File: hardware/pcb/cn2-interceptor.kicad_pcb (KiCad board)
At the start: 2 copper layers, 31.5 x 26 mm, 6 parts, among them J1 JST-XH 4P (CONTROLLER), J2 JST-XH 4P (PANEL), J3 JST-XH 3P (FLOW METER), J4 JST-XH 3P (FV TO CONTROLLER), U1 XIAO ESP32-C3, U2 4CH BSS138 LEVEL SHIFTER

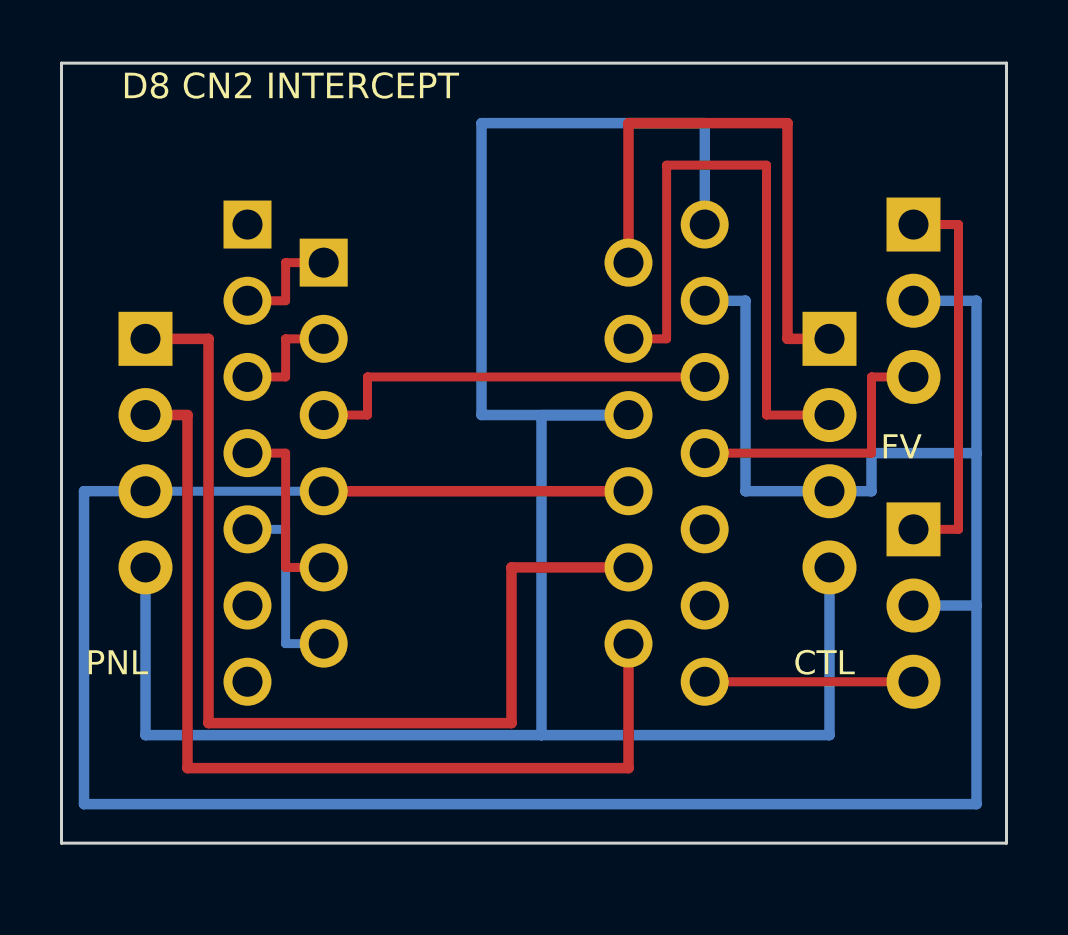
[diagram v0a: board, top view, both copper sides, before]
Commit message: pcb: 18.6 x 27 mm — connectors on opposite edges, flow relay dropped
39% less area and 41% narrower than the 31.5 x 26 board, which is the
dimension that decides whether it fits inside the appliance. Nothing about
the CN2 interception changes.

What made it small: the XIAO's two pad rows are 15.24 mm apart, so anything
standing beside them adds width directly, and the old board had a connector
on each side. Moving both to the top and bottom edges leaves nothing outside
the module except one routing lane -- shared by +5V on top and GND on the
bottom -- so the width is now pad block + lane + two edges, fully accounted
for and with nothing left in it. Each CN2 signal pin sits directly under the
middle corridor and climbs straight out of its own pad into its shifter pin,
turning once, so the four signals need no side lane at all.

The flow-meter relay (J3/J4) is gone, per Kai's call. Its six pins could not
share an edge with the CN2 connectors, so they were what forced the
connectors back onto the sides: that one feature cost more board than
everything else on it. The two hard-won warnings about it (the C3 is not 5 V
tolerant with no channel left to shift FV, and cutting the line strands the
meter's pull-up on the far side) are kept in the README for whoever re-adds
it.

Which connector goes on which edge is load-bearing, not cosmetic. Routing
forces LV1..LV4 onto D1..D4 in order -- they share a 0.94 mm channel and any
other order overlaps four deep -- and D1..D4 are GPIO3,4,5,6. The firmware's
as-built map puts the controller on GPIO5/6, which are the shifter's upper
channels, so the controller enters from the top. Get it backwards and the
board still works but only after swapping four defines, and a pin map that
disagrees with the copper does not announce itself: frames just stop
decoding. gen_pcb.py now reads firmware/include/config.h and fails on a
mismatch rather than leaving that to a comment.

Two new checks, both of which caught something real:

  MECHANICAL  th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
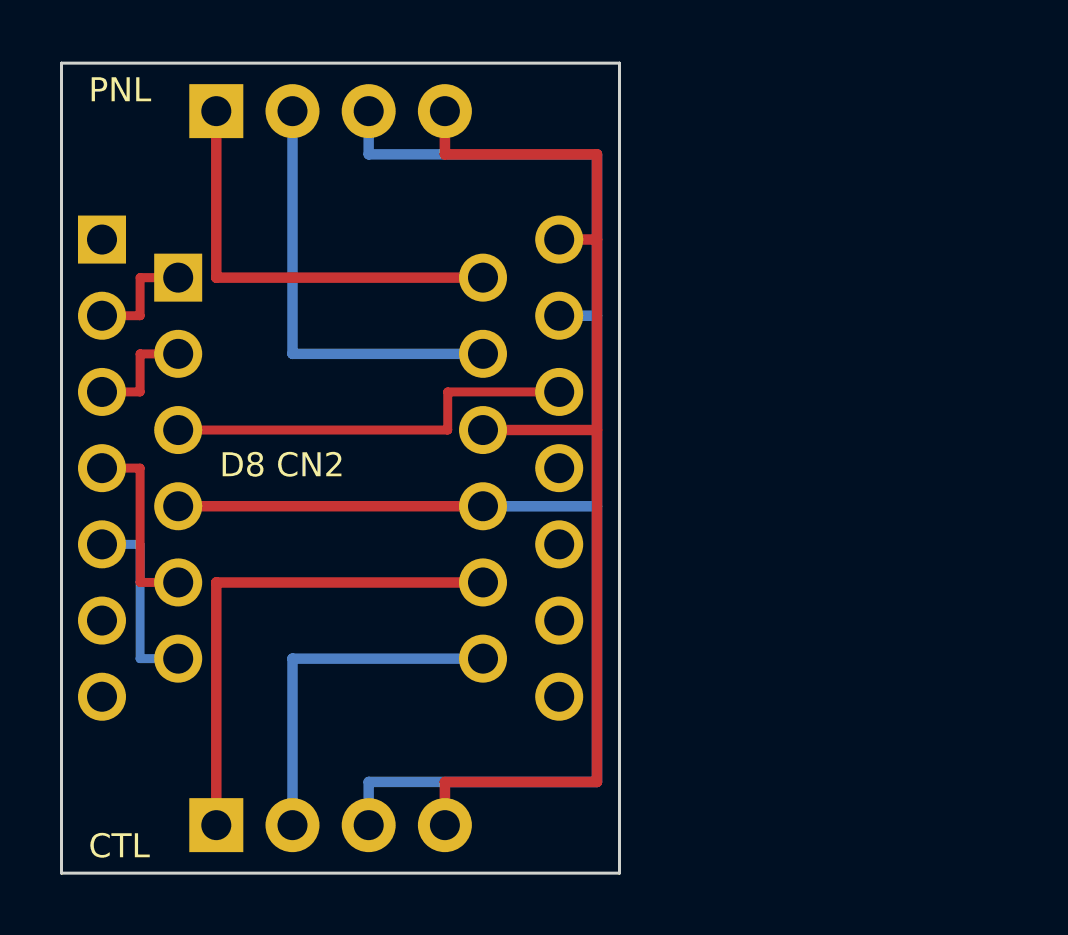
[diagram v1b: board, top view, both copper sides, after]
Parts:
- removed J3: JST-XH 3P (FLOW METER), cn2interceptor:JST_XH_3
- removed J4: JST-XH 3P (FV TO CONTROLLER), cn2interceptor:JST_XH_3
- moved J1 26.1 mm to (5.16, 25.4)
- moved J2 7.95 mm to (5.16, 1.60)
- moved U1 4.88 mm to (1.35, 5.88)
- moved U2 4.88 mm to (3.89, 7.15)
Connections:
- J1 pad 1: CH1_HV -> CH3_HV
- J1 pad 2: CH2_HV -> CH4_HV
- J2 pad 1: CH3_HV -> CH1_HV
- J2 pad 2: CH4_HV -> CH2_HV
- U1 pad D10: FLOW_IN -> (no net)
- U1 pad D7: FLOW_OUT -> (no net)
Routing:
- net GND: track 96.0 -> 54.2 mm
- net +5V: track 73.0 -> 39.0 mm
- net CH4_HV: track 32.0 -> 11.9 mm
- net CH3_HV: track 34.1 -> 17.0 mm
- net FV_VCC: track 13.2 -> 0.00 mm
- net FLOW_IN: track 9.50 -> 0.00 mm
- net FLOW_OUT: track 6.96 -> 0.00 mm
- net CH2_HV: track 20.8 -> 14.4 mm
- net CH1_HV: track 18.5 -> 14.4 mm
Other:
- board size 31.5 x 26 mm -> 18.6 x 27 mm
- board text added: "D8 CN2"
- board text removed: "D8 CN2 INTERCEPT"
- board text removed: "FV"

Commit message: pcb: silkscreen marks the XIAO's USB end and the JST latch side
Two orientation mistakes this board could not previously warn you about, both
of which look correct after assembly:

  USB + arrow   D0 and 5V are the pins at the XIAO's USB end and both sit at
                the low-y end here, so the port faces the PANEL connector.
                A 2x7 header is physically symmetric, so nothing stops the
                module going in backwards -- every signal then lands on the
                wrong pin.
  [ ] bracket   An XH shroud is not symmetric; the ramp the cable clip engages
                is on one long side. Both connectors are marked with the latch
                facing the nearest board edge, so the clips stay reachable once
                the board is mounted. Backwards, the clip faces the board and
                cannot be released.

The silkscreen engine could only draw glyphs, so this adds a Line primitive
and teaches both exporters about it -- the marks would otherwise have appeared
in my Gerbers and the panel but not in the .brd/.kicad_pcb that actually get
imported.

New silk_check(): silkscreen must stay on the board and off every pad. It
caught its own first draft -- the bracket ticks turned outward and ran 0.23 mm
past the edge, where the fab would simply have dropped them. Also bumped the
USB text to 0.8 mm, KiCad's minimum silk height.

Documented while marking it: the USB port faces J2 about 1.4 mm away. On
sockets it clears the JST housing, but a MATED panel cable stands about as
tall as the USB plug and sits right in front. Plug USB in first, or move both
connectors to the top edge (~21 x 24 mm, same area, USB clear). Worth naming
because a session on this project ran entirely over USB serial with the radio
off, so losing USB access after assembly is a real cost.

DRC PASS, connectivity PASS, mechanical PASS, KiCad DRC back to the 4 known
lib_footprint_issues, panel regenerated.

Co-Authored-By: Claude Opus 5 <noreply@anthropic.com>
Cl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
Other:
- board text added: "USB"
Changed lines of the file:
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@@
+      (net 1 "+5V"))
+  )
+  (footprint "cn2interceptor:JST_XH_4" (layer "F.Cu")
+    (at 5.16 25.4)
+    (fp_text reference "J1" (at 0 0) (layer "F.Fab")
+        (effects (font (size 1.27 1.27) (thickness 0.15)))
+    )
+    (fp_text value "JST-XH 4P (CONTROLLER)" (at 0 0) (layer "F.Fab")
+        (effects (font (size 1.27 1.27) (thickness 0.15)))
+    )
+    (pad "1" thru_hole rect (at 0 0) (size 1.8 1.8) (drill 1) (layers "*.Cu" "*.Mask")
+      (net 8 "CH3_HV") (thermal_bridge_angle 45))
+    (pad "2" thru_hole circle (at 2.54 0) (size 1.8 1.8) (drill 1) (layers "*.Cu" "*.Mask")
+      (net 10 "CH4_HV"))
+    (pad "3" thru_hole circle (at 5.08 0) (size 1.8 1.8) (drill 1) (layers "*.Cu" "*.Mask")
+      (net 2 "GND"))
+    (pad "4" thru_hole circle (at 7.62 0) (size 1.8 1.8) (drill 1) (layers "*.Cu" "*.Mask")
       (net 1 "+5V"))
   )
@@
       (net 11 "CH4_LV"))
   )
-  (footprint "cn2interceptor:JST_XH_4" (layer "F.Cu")
-    (at 5.16 25.4)
-    (fp_text reference "J1" (at 0 0) (layer "F.Fab")
-        (effects (font (size 1.27 1.27) (thickness 0.15)))
-    )
-    (fp_text value "JST-XH 4P (CONTROLLER)" (at 0 0) (layer "F.Fab")
-        (effects (font (size 1.27 1.27) (thickness 0.15)))
-    )
-    (pad "1" thru_hole rect (at 0 0) (size 1.8 1.8) (drill 1) (layers "*.Cu" "*.Mask")
-      (net 8 "CH3_HV") (thermal_bridge_angle 45))
-    (pad "2" thru_hole circle (at 2.54 0) (size 1.8 1.8) (drill 1) (layers "*.Cu" "*.Mask")
-      (net 10 "CH4_HV"))
-    (pad "3" thru_hole circle (at 5.08 0) (size 1.8 1.8) (drill 1) (layers "*.Cu" "*.Mask")
-      (net 2 "GND"))
-    (pad "4" thru_hole circle (at 7.62 0) (size 1.8 1.8) (drill 1) (layers "*.Cu" "*.Mask")
-      (net 1 "+5V"))
-  )
+  (gr_line (start 3.9 0.32) (end 3.9 0.87)
+    (stroke (width 0.15) (type default)) (layer "F.SilkS"))
+  (gr_line (start 14.04 26.68) (end 14.04 26.13)
+    (stroke (width 0.15) (type default)) (layer "F.SilkS"))
+  (gr_line (start 14.04 0.32) (end 14.04 0.87)
+    (stroke (width 0.15) (type default)) (layer "F.SilkS"))
+  (gr_line (start 17.15 0.45) (end 16.55 1.45)
+    (stroke (width 0.15) (type default)) (layer "F.SilkS"))
+  (gr_line (start 3.9 26.68) (end 3.9 26.13)
+    (stroke (width 0.15) (type default)) (layer "F.SilkS"))
+  (gr_line (start 3.9 0.32) (end 14.04 0.32)
+    (stroke (width 0.15) (type default)) (layer "F.SilkS"))
+  (gr_line (start 3.9 26.68) (end 14.04 26.68)
+    (stroke (width 0.15) (type default)) (layer "F.SilkS"))
+  (gr_line (start 17.15 0.45) (end 17.15 2.35)
+    (stroke (width 0.15) (type default)) (layer "F.SilkS"))
+  (gr_line (start 17.15 0.45) (end 17.75 1.45)
+    (stroke (width 0.15) (type default)) (layer "F.SilkS"))
+  (gr_line (start 16.55 1.45) (end 17.75 1.45)
+    (stroke (width 0.15) (type default)) (layer "F.SilkS"))
+  (gr_line (start 18.6 0) (end 18.6 27)
+    (stroke (width 0.1) (type default)) (layer "Edge.Cuts"))
   (gr_line (start 0 27) (end 0 0)
-    (stroke (width 0.1) (type default)) (layer "Edge.Cuts"))
-  (gr_line (start 18.6 0) (end 18.6 27)
     (stroke (width 0.1) (type default)) (layer "Edge.Cuts"))
   (gr_line (start 0 0) (end 18.6 0)
@@
   (gr_line (start 18.6 27) (end 0 27)
     (stroke (width 0.1) (type default)) (layer "Edge.Cuts"))
-  (gr_text "D8 CN2" (at 5.265 13.4) (layer "F.SilkS")
+  (gr_text "CTL" (at 0.9 26.099999) (layer "F.SilkS")
     (effects (font (size 0.8 0.8) (thickness 0.15)) (justify left))
   )
@@
     (effects (font (size 0.8 0.8) (thickness 0.15)) (justify left))
   )
-  (gr_text "CTL" (at 0.9 26.099999) (layer "F.SilkS")
+  (gr_text "USB" (at 13.95 1.3) (layer "F.SilkS")
     (effects (font (size 0.8 0.8) (thickness 0.15)) (justify left))
   )
+  (gr_text "D8 CN2" (at 5.265 13.4) (layer "F.SilkS")
+    (effects (font (size 0.8 0.8) (thickness 0.15)) (justify left))
+  )
+  (segment (start 12.78 23.96) (end 17.85 23.96) (width 0.35) (layer "F.Cu") (net 1))
+  (segment (start 17.85 23.96) (end 17.85 12.23) (width 0.35) (layer "F.Cu") (net 1))
+  (segment (start 17.85 5.88) (end 16.59 5.88) (width 0.35) (layer "F.Cu") (net 1))
+  (segment (start 12.78 3.04) (end 17.85 3.04) (width 0.35) (layer "F.Cu") (net 1))
+  (segment (start 17.85 3.04) (end 17.85 5.88) (width 0.35) (layer "F.Cu") (net 1))
+  (segment (start 17.85 12.23) (end 14.05 12.23) (width 0.35) (layer "F.Cu") (net 1))
+  (segment (start 17.85 5.88) (end 17.85 12.23) (width 0.35) (layer "F.Cu") (net 1))
+  (segment (start 12.78 25.4) (end 12.78 23.96) (width 0.35) (layer "F.Cu") (net 1))
   (segment (start 12.78 1.6) (end 12.78 3.04) (width 0.35) (layer "F.Cu") (net 1))
-  (segment (start 17.85 5.88) (end 16.59 5.88) (width 0.35) (layer "F.Cu") (net 1))
-  (segment (start 12.78 25.4) (end 12.78 23.96) (width 0.35) (layer "F.Cu") (net 1))
-  (segment (start 17.85 5.88) (end 17.85 12.23) (width 0.35) (layer "F.Cu") (net 1))
-  (segment (start 17.85 12.23) (end 14.05 12.23) (width 0.35) (layer "F.Cu") (net 1))
-  (segment (start 12.78 3.04) (end 17.85 3.04) (width 0.35) (layer "F.Cu") (net 1))
-  (segment (start 12.78 23.96) (end 17.85 23.96) (width 0.35) (layer "F.Cu") (net 1))
-  (segment (start 17.85 3.04) (end 17.85 5.88) (width 0.35) (layer "F.Cu") (net 1))
-  (segment (start 17.85 23.96) (end 17.85 12.23) (width 0.35) (layer "F.Cu") (net 1))
   (segment (start 14.05 14.77) (end 3.89 14.77) (width 0.35) (layer "F.Cu") (net 2))
-  (segment (start 17.85 14.77) (end 14.05 14.77) (width 0.35) (layer "B.Cu") (net 2))
-  (segment (start 10.24 23.96) (end 17.85 23.96) (width 0.35) (layer "B.Cu") (net 2))
-  (segment (start 17.85 8.42) (end 17.85 14.77) (width 0.35) (layer "B.Cu") (net 2))
   (segment (start 17.85 23.96) (end 17.85 14.77) (width 0.35) (layer "B.Cu") (net 2))
   (segment (start 10.24 25.4) (end 10.24 23.96) (width 0.35) (layer "B.Cu") (net 2))
   (segment (start 10.24 1.6) (end 10.24 3.04) (width 0.35) (layer "B.Cu") (net 2))
+  (segment (start 10.24 23.96) (end 17.85 23.96) (width 0.35) (layer "B.Cu") (net 2))
+  (segment (start 10.24 3.04) (end 17.85 3.04) (width 0.35) (layer "B.Cu") (net 2))
   (segment (start 17.85 8.42) (end 16.59 8.42) (width 0.35) (layer "B.Cu") (net 2))
   (segment (start 17.85 3.04) (end 17.85 8.42) (width 0.35) (layer "B.Cu") (net 2))
-  (segment (start 10.24 3.04) (end 17.85 3.04) (width 0.35) (layer "B.Cu") (net 2))
+  (segment (start 17.85 14.77) (end 14.05 14.77) (width 0.35) (layer "B.Cu") (net 2))
+  (segment (start 17.85 8.42) (end 17.85 14.77) (width 0.35) (layer "B.Cu") (net 2))
+  (segment (start 12.875 10.96) (end 16.59 10.96) (width 0.3) (layer "F.Cu") (net 3))
+  (segment (start 12.875 12.23) (end 12.875 10.96) (width 0.3) (layer "F.Cu") (net 3))
   (segment (start 3.89 12.23) (end 12.875 12.23) (width 0.3) (layer "F.Cu") (net 3))
-  (segment (start 12.875 12.23) (end 12.875 10.96) (width 0.3) (layer "F.Cu") (net 3))
-  (segment (start 12.875 10.96) (end 16.59 10.96) (width 0.3) (layer "F.Cu") (net 3))
+  (segment (start 5.16 7.15) (end 14.05 7.15) (width 0.35) (layer "F.Cu") (net 4))
   (segment (start 5.16 1.6) (end 5.16 7.15) (width 0.35) (layer "F.Cu") (net 4))
-  (segment (start 5.16 7.15) (end 14.05 7.15) (width 0.35) (layer "F.Cu") (net 4))
+  (segment (start 2.62 7.15) (end 2.62 8.42) (width 0.3) (layer "F.Cu") (net 5))
+  (segment (start 2.62 8.42) (end 1.35 8.42) (width 0.3) (layer "F.Cu") (net 5))
   (segment (start 3.89 7.15) (end 2.62 7.15) (width 0.3) (layer "F.Cu") (net 5))
-  (segment (start 2.62 8.42) (end 1.35 8.42) (width 0.3) (layer "F.Cu") (net 5))
-  (segment (start 2.62 7.15) (end 2.62 8.42) (width 0.3) (layer "F.Cu") (net 5))
+  (segment (start 7.7 9.69) (end 14.05 9.69) (width 0.35) (layer "B.Cu") (net 6))
   (segment (start 7.7 1.6) (end 7.7 9.69) (width 0.35) (layer "B.Cu") (net 6))
-  (segment (start 7.7 9.69) (end 14.05 9.69) (width 0.35) (layer "B.Cu") (net 6))
+  (segment (start 2.62 9.69) (end 2.62 10.96) (width 0.3) (layer "F.Cu") (net 7))
+  (segment (start 3.89 9.69) (end 2.62 9.69) (width 0.3) (layer "F.Cu") (net 7))
   (segment (start 2.62 10.96) (end 1.35 10.96) (width 0.3) (layer "F.Cu") (net 7))
-  (segment (start 3.89 9.69) (end 2.62 9.69) (width 0.3) (layer "F.Cu") (net 7))
-  (segment (start 2.62 9.69) (end 2.62 10.96) (width 0.3) (layer "F.Cu") (net 7))
+  (segment (start 5.16 17.31) (end 14.05 17.31) (width 0.35) (layer "F.Cu") (net 8))
   (segment (start 5.16 25.4) (end 5.16 17.31) (width 0.35) (layer "F.Cu") (net 8))
-  (segment (start 5.16 17.31) (end 14.05 17.31) (width 0.35) (layer "F.Cu") (net 8))
+  (segment (start 2.62 17.31) (end 2.62 13.5) (width 0.3) (layer "F.Cu") (net 9))
   (segment (start 3.89 17.31) (end 2.62 17.31) (width 0.3) (layer "F.Cu") (net 9))
-  (segment (start 2.62 17.31) (end 2.62 13.5) (width 0.3) (layer "F.Cu") (net 9))
   (segment (start 2.62 13.5) (end 1.35 13.5) (width 0.3) (layer "F.Cu") (net 9))
   (segment (start 7.7 19.85) (end 14.05 19.85) (width 0.35) (layer "B.Cu") (net 10))
   (segment (start 7.7 25.4) (end 7.7 19.85) (width 0.35) (layer "B.Cu") (net 10))
+  (segment (start 2.62 19.85) (end 2.62 16.04) (width 0.3) (layer "B.Cu") (net 11))
   (segment (start 3.89 19.85) (end 2.62 19.85) (width 0.3) (layer "B.Cu") (net 11))
   (segment (start 2.62 16.04) (end 1.35 16.04) (width 0.3) (layer "B.Cu") (net 11))
-  (segment (start 2.62 19.85) (end 2.62 16.04) (width 0.3) (layer "B.Cu") (net 11))
 )
